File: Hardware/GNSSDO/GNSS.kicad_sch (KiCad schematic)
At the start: 50 parts, among them J1 SMA_Edge, J6 microSD, U13 SiT5358AI-FS033IT-10.000000, U2 mosaic-T

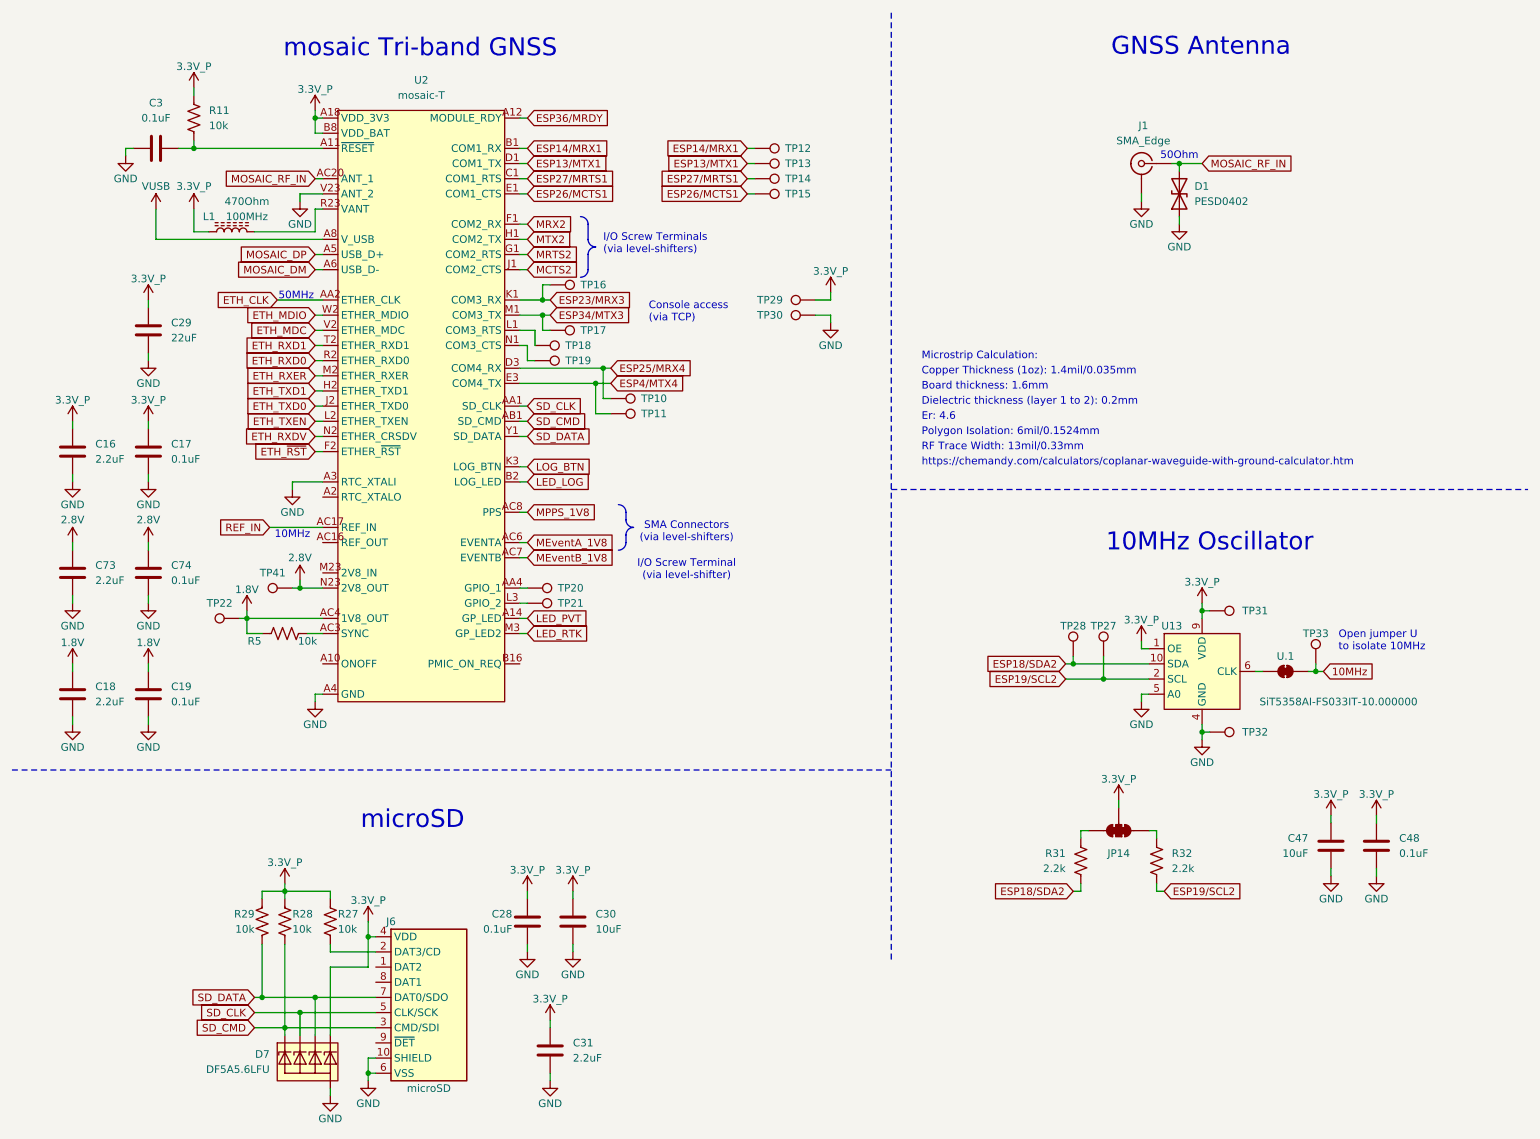
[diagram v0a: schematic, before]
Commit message: KiCad 10
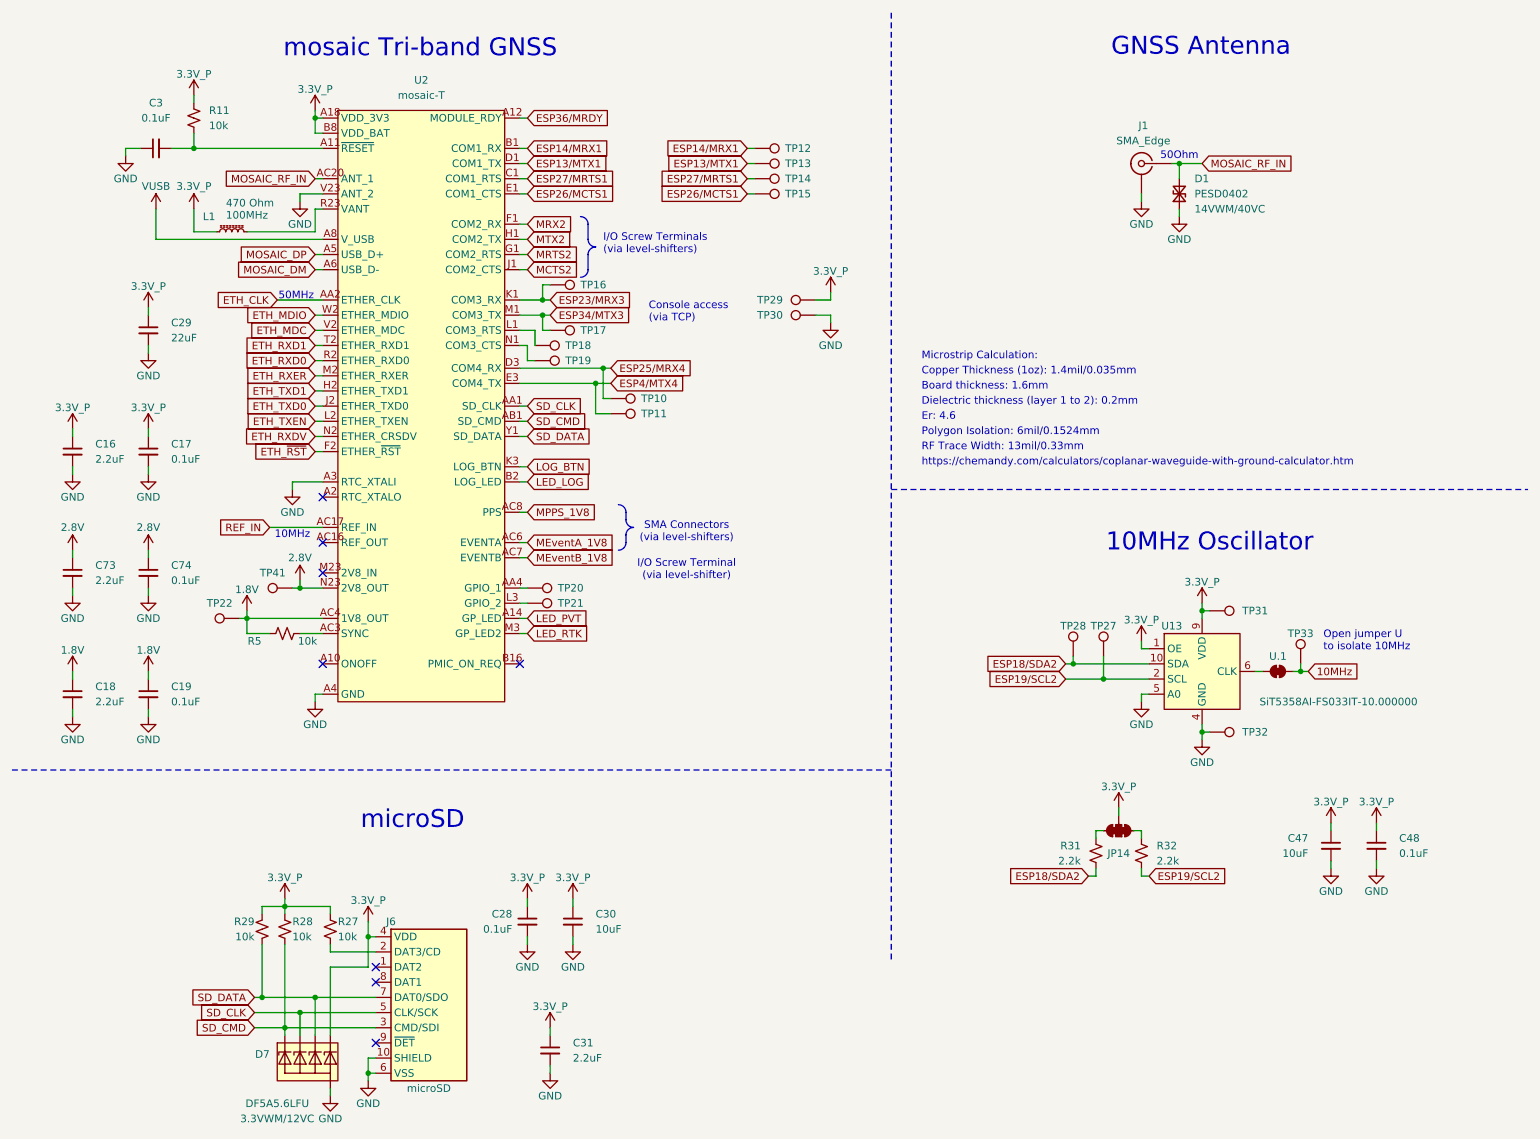
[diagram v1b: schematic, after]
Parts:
- C16, C18, C31, C73: PROD_ID CAP-07888 -> CAP-24999
- D1: symbol SparkFun-DiscreteSemi:D_TVS_0402 -> SparkFun-DiscreteSemi:D_TVS_0402_14V; Rating (none) -> 14VWM/40VC
- D7: symbol SparkFun-DiscreteSemi:D_TVS_ESD_4_HS -> SparkFun-DiscreteSemi:D_TVS_ESD_4_HS_3.3V; Rating (none) -> 3.3VWM/12VC
- J1: footprint SparkFun-Connector:SMA_Edge -> SparkFun-Connector:SMA_Edge_6.3mm; symbol SparkFun-RF:SMA_EdgeMount -> SparkFun-RF:SMA_EdgeMount_6.3mm
- JP14, U.1: value ~ -> (none)
- L1: value 470Ohm -> 470 Ohm; symbol SparkFun-Coil:470Ohm_0603_1.0A -> SparkFun-Coil:Ferrite_470Ohm_0603_1.0A
- TP10, TP11, TP12, TP13, TP14, TP15, TP16, TP17, TP18, TP19, TP20, TP21, TP22, TP27, TP28, TP29, TP30, TP31, TP32, TP33, TP41: footprint SparkFun-Connector:1x01 -> SparkFun-Connector:1x01_P2.54mm
- U2: footprint SparkFun-GPS:MOSAIC_LGA -> SparkFun-GNSS:Septentrio_mosaic_LGA; symbol SparkFun-GPS:mosaic-T -> SparkFun-GNSS:mosaic-T
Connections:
- net 1.8V: now also R5.1; no longer R5.2
- net 3.3V_P: now also R11.1, R27.1, R28.1, R29.1; no longer R11.2, R27.2, R28.2, R29.2
- net ESP18/SDA2: now also R31.1; no longer R31.2
- net ESP19/SCL2: now also R32.1; no longer R32.2
- net SD_CMD: now also R28.2; no longer R28.1
- net SD_DATA: now also R29.2; no longer R29.1
- net at C3.2, U2.A11 (~{RESET}): now also R11.2; no longer R11.1
- net at U2.AC3 (SYNC): now also R5.2; no longer R5.1
- net at JP14.1 (A): now also R32.2; no longer R32.1
- net at JP14.3 (C): now also R31.2; no longer R31.1
- net at J6.2 (DAT3/CD): now also R27.2; no longer R27.1
- no-connect marks 0 -> 8
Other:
- moved on the sheet: JP14, TP33, U.1
